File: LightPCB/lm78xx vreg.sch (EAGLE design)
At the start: 15 parts, among them IC1 7805TV, J1 +18v

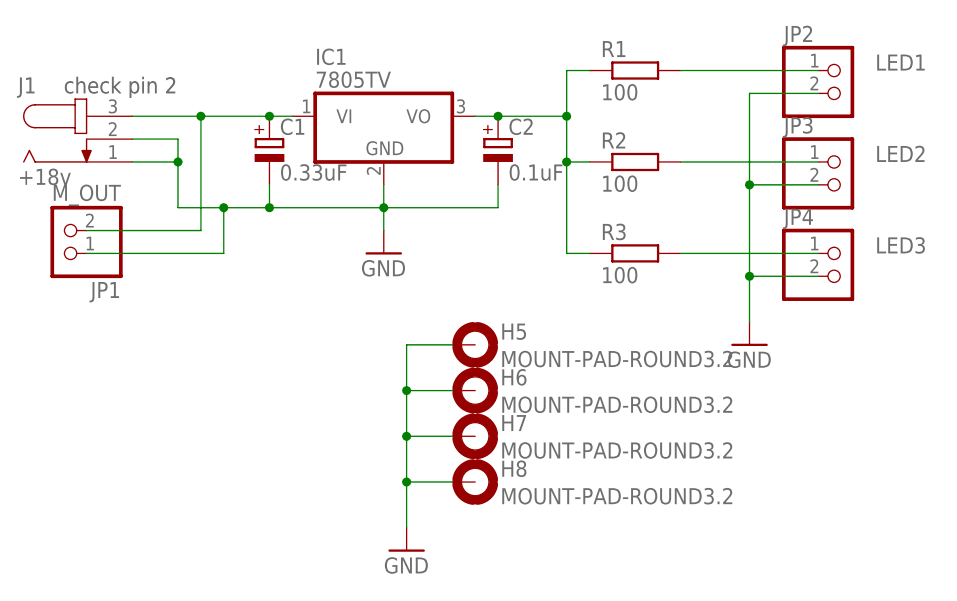
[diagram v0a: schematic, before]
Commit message: Changed DRC for light PCB
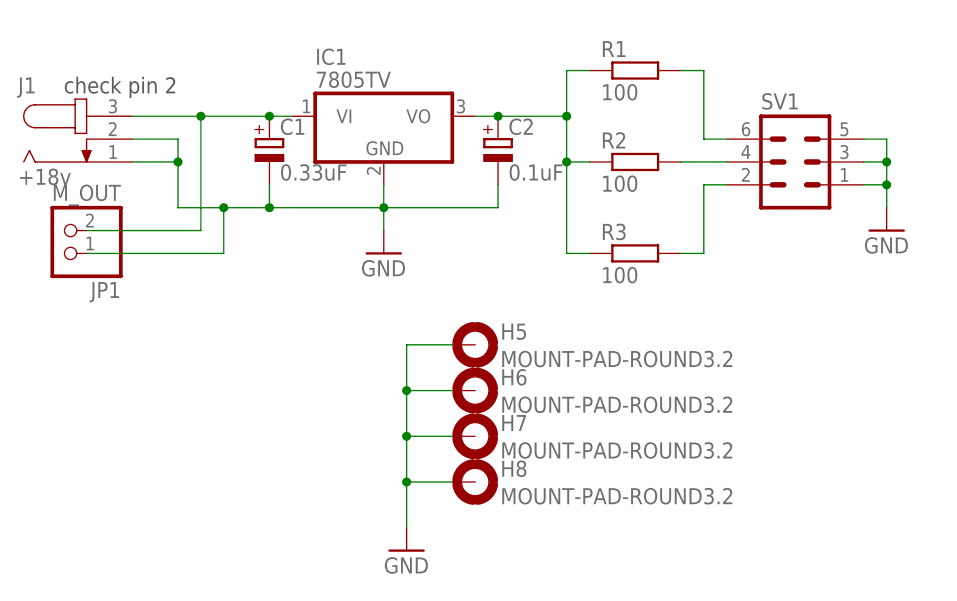
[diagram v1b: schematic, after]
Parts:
- removed JP2: LED1, pinhead:PINHD-1X2
- removed JP3: LED2, pinhead:PINHD-1X2
- removed JP4: LED3, pinhead:PINHD-1X2
- added SV1: (no value), con-lstb:MA03-2
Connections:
- removed net N$6: JP2.1, R1.2
- removed net N$7: JP3.1, R2.2
- removed net N$8: JP4.1, R3.2
- new net N$3: R2.2, SV1.4
- new net N$4: R1.2, SV1.6
- new net N$5: R3.2, SV1.2
- net GND: now also SV1.1, SV1.3, SV1.5; no longer JP2.2, JP3.2, JP4.2
